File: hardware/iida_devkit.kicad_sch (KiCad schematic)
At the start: 7 parts

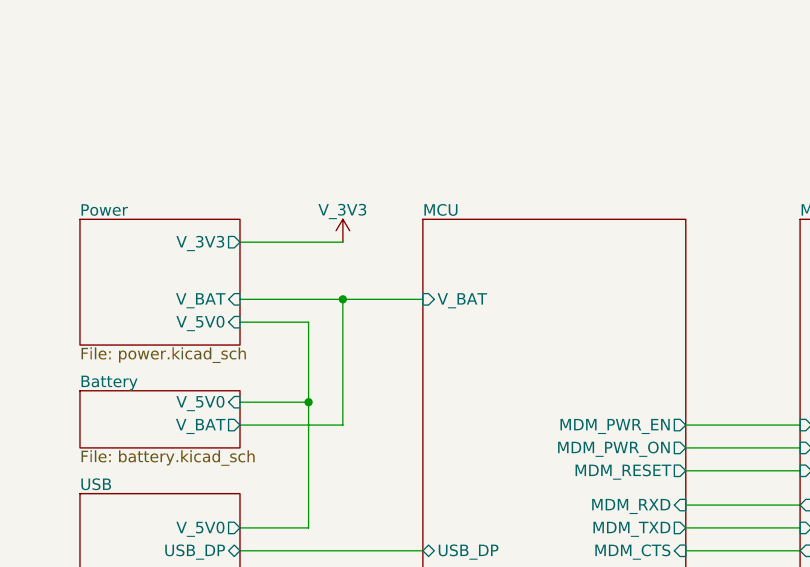
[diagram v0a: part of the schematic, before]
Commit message: HW: Add global V_BAT
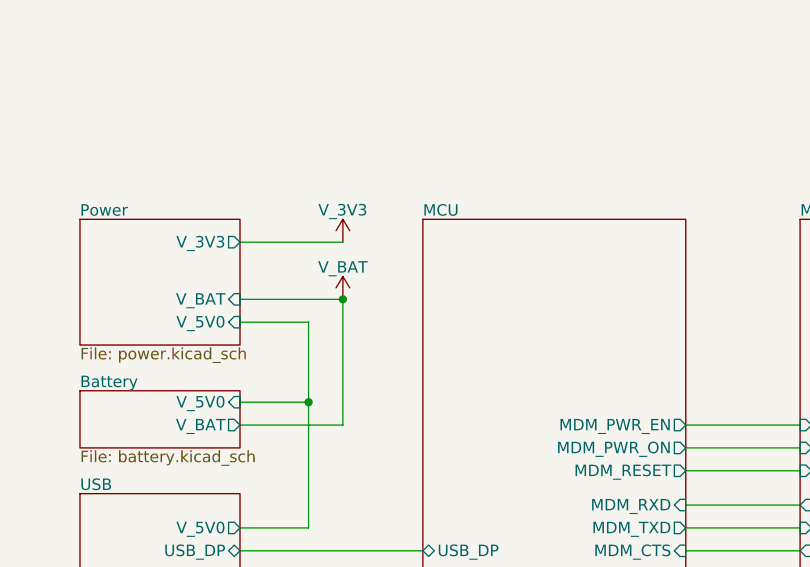
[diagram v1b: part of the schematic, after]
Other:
- sheet MCU ports: added none; removed V_BAT
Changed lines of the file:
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@@
-	(wire
-		(pts
-			(xy 270.51 110.49) (xy 279.4 110.49)
-		)
-		(stroke
-			(width 0)
-			(type default)
-		)
-	)
 	(wire
 		(pts
@@
 				(path "/b12a6e25-97fb-4aba-bc96-af8db389bb9a"
 					(reference "H1")
+					(unit 1)
+				)
+			)
+		)
+	)
+	(symbol
+		(lib_id "power:+BATT")
+		(at 270.51 110.49 0)
+		(unit 1)
+		(exclude_from_sim no)
+		(in_bom yes)
+		(on_board yes)
+		(dnp no)
+		(property "Reference" "#PWR0108"
+			(at 270.51 114.3 0)
+			(effects
+				(font
+					(size 1.27 1.27)
+				)
+				(hide yes)
+			)
+		)
+		(property "Value" "V_BAT"
+			(at 270.51 106.934 0)
+			(effects
+				(font
+					(size 1.27 1.27)
+				)
+			)
+		)
+		(property "Footprint" ""
+			(at 270.51 110.49 0)
+			(effects
+				(font
+					(size 1.27 1.27)
+				)
+				(hide yes)
+			)
+		)
+		(property "Datasheet" ""
+			(at 270.51 110.49 0)
+			(effects
+				(font
+					(size 1.27 1.27)
+				)
+				(hide yes)
+			)
+		)
+		(property "Description" ""
+			(at 270.51 110.49 0)
+			(effects
+				(font
+					(size 1.27 1.27)
+				)
+				(hide yes)
+			)
+		)
+		(pin "1"
+		)
+		(instances
+			(project ""
+				(path "/b12a6e25-97fb-4aba-bc96-af8db389bb9a"
+					(reference "#PWR0108")
 					(unit 1)
 				)
@@
 			)
 		)
-		(pin "V_BAT" input
-			(at 279.4 110.49 180)
-			(effects
-				(font
-					(size 1.27 1.27)
-				)
-				(justify left)
-			)
-		)

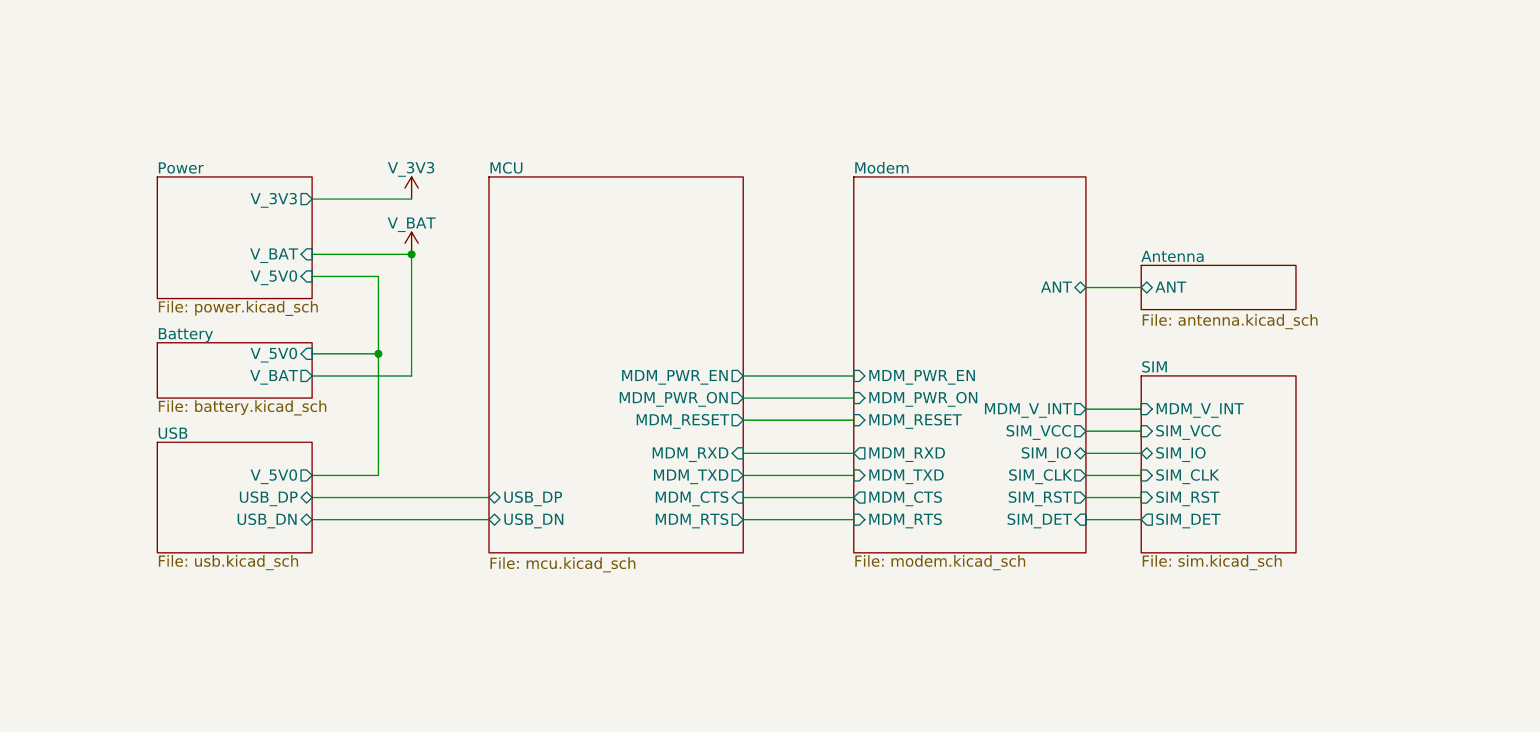
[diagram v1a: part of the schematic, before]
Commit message: HW: Add global symbols for V_BAT and V_5V0
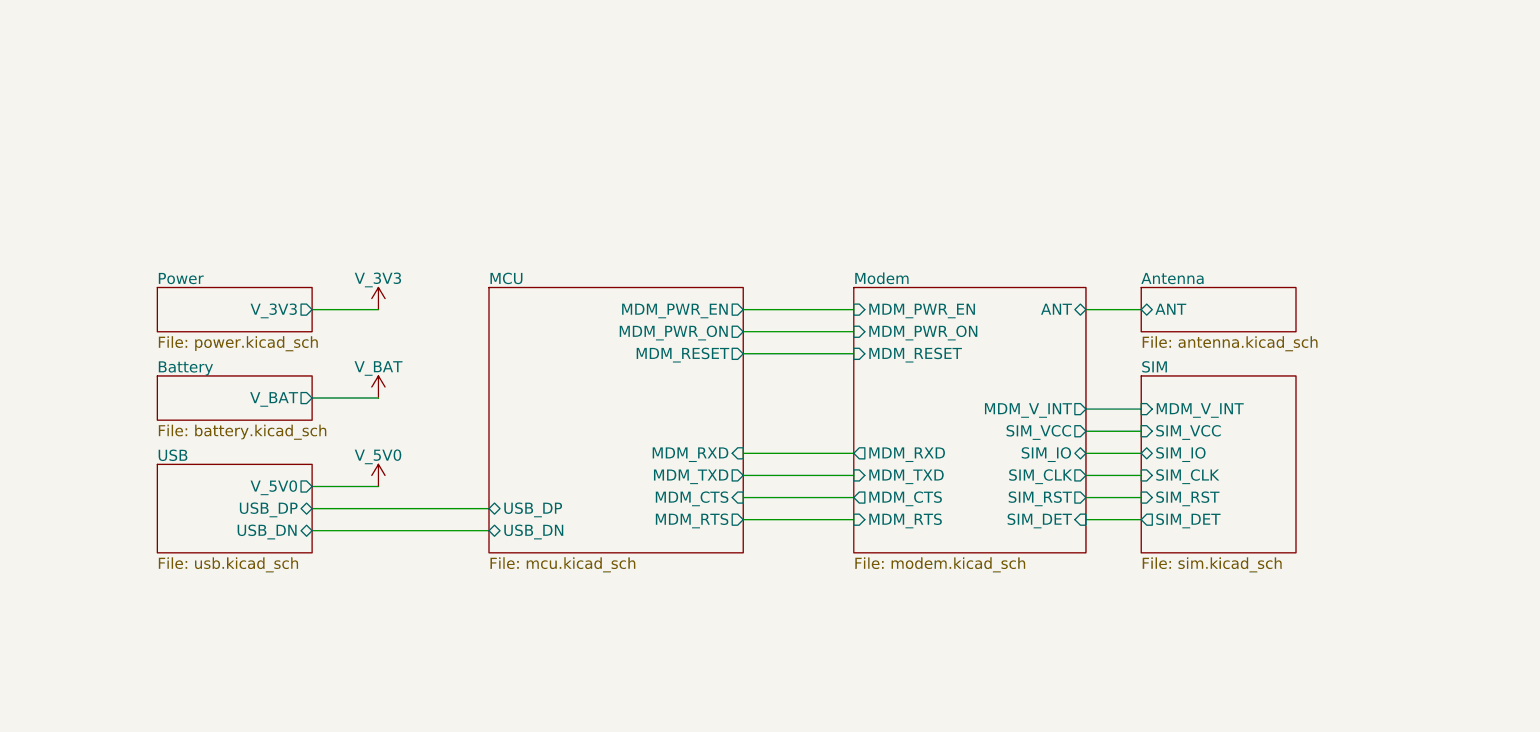
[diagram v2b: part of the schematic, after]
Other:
- sheet Battery ports: added none; removed V_5V0
- sheet Power ports: added none; removed V_5V0, V_BAT

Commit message: HW: Improve comments
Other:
- note added: "Place a stitched ground guard rail along the edges of the PCB to provide a grounding point for human contact when handling the device."
- note added: "Place fiducials at the top-left, bottom-left, and bottom-right corners of the PCB."
- note added: "There's no actual chassis or case for mounting the PCB, so just place the mounting holes at the corners of the board."
- note added: "This project serves as a practice exercise in PCB design and embedded programming. The result is a device that can be powered either by a battery or via a USB connection. The device is capable of recharging the battery through the USB interface. Key features of the device include: - A sample sensor (temperature) - External flash memory to support firmware-over-the-air (FOTA) updates - A modem mod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"
- note removed: "Place a stitched GND guard rail around the edges of the PCB to provide a grounding point for human touch when handling the device."
- note removed: "Place fiducials at three corners of the PCB."
- note removed: "There's no real chassis or a case to mount the PCB, so just place the mounting holes at the corners of the PCB."
- note removed: "This is a project for practicing PCB design and programming. The result is a device that is powered either with a battery or with a USB connection. The device can recharge the battery via the USB connection. The device includes: - An example sensor (temperature) - External flash for updating the firmware over the air (FOTA) - A modem module that connects the main microcontroller to the internet w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"
- moved on the sheet: FID1, FID2, FID3
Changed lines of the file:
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@@
 		)
 	)
-	(text "There's no real chassis or a case to mount the PCB,\nso just place the mounting holes at the corners of the PCB."
+	(text "There's no actual chassis or case for mounting the PCB,\nso just place the mounting holes at the corners of the board."
 		(exclude_from_sim no)
 		(at 205.74 228.6 0)
@@
 		)
 	)
-	(text "Place fiducials at three corners of the PCB."
+	(text "Place fiducials at the top-left, bottom-left,\nand bottom-right corners of the PCB."
 		(exclude_from_sim no)
 		(at 279.4 228.6 0)
@@
 		)
 	)
-	(text "This is a project for practicing PCB design and programming.\n\nThe result is a device that is powered either with a battery or with a USB connection.\nThe device can recharge the battery via the USB connection.\n\nThe device includes:\n  - An example sensor (temperature)\n  - External flash for updating the firmware over the air (FOTA)\n  - A modem module that connects the main microcontroller to the internet with LTE CAT-M1\n  - Option to use either an external antenna or an integrated antenna\n\nA key goal of the project is to ensure it has as little reliance as possible on totalitarian\ncountries (e.g., China or Russia) or on hostile countries (e.g., USA).\nComponent sourcing must be done carefully to select manufacturers who can supply parts\nthat are not produced in such countries.\nInstead, democratic countries (e.g., Taiwan and Germany) should be preferred.\n\nTo reduce strain on the global environment, manufacturing and sourcing is centered around\nEurope.\n\nFor manufacturing, the following companies are recommended:\n- Aisler (Germany)\n- Aspocomp? (Finland)\n\nFor components, the following companies are recommended:\n- Würth Elektronik (Germany)\n- Infineon Technologies (Germany)\n- STMicroelectronics (Italy)\n\nFor suppliers, the following companies are recommended:\n- Transfer Multisort Elektronik (Poland)\n- RS Components (England)"
+	(text "This project serves as a practice exercise in PCB design and embedded programming.\n\nThe result is a device that can be powered either by a battery or via a USB connection.\nThe device is capable of recharging the battery through the USB interface.\n\nKey features of the device include:\n- A sample sensor (temperature)\n- External flash memory to support firmware-over-the-air (FOTA) updates\n- A modem module that connects the main microcontroller to the internet via LTE CAT-M1\n- Support for both an external antenna and an integrated antenna\n\nA primary objective of this project is to minimize reliance on totalitarian states\n(e.g., China or Russia) and on countries that may be hostile (e.g., the United States).\nComponent sourcing should prioritize manufacturers that do not produce\ncomponents in such countries.\nPreference should be given to suppliers and manufacturers based in democratic nations,\nsuch as Taiwan and Germany.\n\nTo help reduce environmental impact, both manufacturing and component sourcing are\nfocused around Europe.\n\nRecommended manufacturers:\n- Aisler (Germany)\n- Multi CB (Germany)\n- Aspocomp (Finland)\n\nRecommended component manufacturers:\n- Würth Elektronik (Germany)\n- Infineon Technologies (Germany)\n- STMicroelectronics (Italy)\n\nRecommended distributors:\n- Transfer Multisort Elektronik (Poland)\n- RS Components (United Kingdom)\n- Farnell (United Kingdom)"
 		(exclude_from_sim no)
 		(at 15.24 63.5 0)
@@
 		)
 	)
-	(text "Place a stitched GND guard rail around the edges of the PCB\nto provide a grounding point for human touch when handling the device."
+	(text "Place a stitched ground guard rail along the edges of the PCB\nto provide a grounding point for human contact when handling the device."
 		(exclude_from_sim no)
 		(at 330.2 228.6 0)
@@
 	(symbol
 		(lib_id "Mechanical:Fiducial")
-		(at 299.72 234.95 0)
+		(at 299.72 241.3 0)
 		(unit 1)
 		(exclude_from_sim no)
@@
 		(dnp no)
 		(property "Reference" "FID2"
-			(at 299.72 232.156 0)
+			(at 299.72 238.506 0)
 			(effects
 				(font
@@
 		)
 		(property "Value" "Fiducial"
-			(at 302.26 236.2199 0)
+			(at 302.26 242.5699 0)
 			(effects
 				(font
@@
 		)
 		(property "Footprint" "Fiducial:Fiducial_1mm_Mask2mm"
-			(at 299.72 234.95 0)
+			(at 299.72 241.3 0)
 			(effects
 				(font
@@
 		)
 		(property "Datasheet" "~"
-			(at 299.72 234.95 0)
+			(at 299.72 241.3 0)
 			(effects
 				(font
@@
 		)
 		(property "Description" "Fiducial Marker"
-			(at 299.72 234.95 0)
+			(at 299.72 241.3 0)
 			(effects
 				(font
@@
 	(symbol
 		(lib_id "Mechanical:Fiducial")
-		(at 287.02 234.95 0)
+		(at 287.02 241.3 0)
 		(unit 1)
 		(exclude_from_sim no)
@@
 		(dnp no)
 		(property "Reference" "FID1"
-			(at 287.02 232.156 0)
+			(at 287.02 238.506 0)
 			(effects
 				(font
@@
 		)
 		(property "Value" "Fiducial"
-			(at 289.56 236.2199 0)
+			(at 289.56 242.5699 0)
 			(effects
 				(font
@@
 		)
 		(property "Footprint" "Fiducial:Fiducial_1mm_Mask2mm"
-			(at 287.02 234.95 0)
+			(at 287.02 241.3 0)
 			(effects
 				(font
@@
 		)
 		(property "Datasheet" "~"
-			(at 287.02 234.95 0)
+			(at 287.02 241.3 0)
 			(effects
 				(font
@@
 		)
 		(property "Description" "Fiducial Marker"
-			(at 287.02 234.95 0)
+			(at 287.02 241.3 0)
 			(effects
 				(font
@@
 	(symbol
 		(lib_id "Mechanical:Fiducial")
-		(at 312.42 234.95 0)
+		(at 312.42 241.3 0)
 		(unit 1)
 		(exclude_from_sim no)
@@
 		(dnp no)
 		(property "Reference" "FID3"
-			(at 312.42 232.156 0)
+			(at 312.42 238.506 0)
 			(effects
 				(font
@@
 		)
 		(property "Value" "Fiducial"
-			(at 314.96 236.2199 0)
+			(at 314.96 242.5699 0)
 			(effects
 				(font
@@
 		)
 		(property "Footprint" "Fiducial:Fiducial_1mm_Mask2mm"
-			(at 312.42 234.95 0)
+			(at 312.42 241.3 0)
 			(effects
 				(font
@@
 		)
 		(property "Datasheet" "~"
-			(at 312.42 234.95 0)
+			(at 312.42 241.3 0)
 			(effects
 				(font
@@
 		)
 		(property "Description" "Fiducial Marker"
-			(at 312.42 234.95 0)
-			(effects
-				(font
+			(at 312.42 241.3 0)
+			(effects
+				(font
